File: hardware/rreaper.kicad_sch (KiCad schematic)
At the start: 0 parts

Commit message: added basic hardware schematic
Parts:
- added C11, C22, C31, C41: 100n, symbol Device:C_Small
- added C12: 1u, symbol Device:C_Small
- added C21: 220n, symbol Device:C_Small
- added CJ1: 100n, Capacitor_SMD:C_0805_2012Metric_Pad1.18x1.45mm_HandSolder, symbol Device:C
- added CX1, CX2: 22p, symbol Device:C_Small
- added J1: ZIF, symbol Connector_Generic:Conn_02x14_Counter_Clockwise
- added J2: USB_B_Micro, Connector_USB:USB_Micro-B_Wuerth_629105150521_CircularHoles, symbol Connector:USB_B_Micro
- added J3: ICP, Connector_IDC:IDC-Header_2x05_P2.54mm_Vertical, symbol Connector_Generic:Conn_02x05_Odd_Even
- added R1, R11, R2: 4k7, symbol Device:R_Small
- added U1: ATmega328P, PCM_Package_DIP_AKL:DIP-28_W7.62mm_Socket, symbol MCU_Microchip_ATmega:ATmega328P-P
- added U2: MCP2221A, PCM_Package_DIP_AKL:DIP-14_W7.62mm_Socket, symbol Interface_USB:MCP2221AxP
- added U3, U4: 74HC595, PCM_Package_DIP_AKL:DIP-16_W7.62mm_Socket, symbol 74xx:74HC595
- added X1: 16MHz, symbol PCM_Crystal_AKL:Crystal_Generic
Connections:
- new net: CX1.1, U1.9 (XTAL1/PB6), X1.1
- new net: CX2.1, U1.10 (XTAL2/PB7), X1.2
- new net: R1.1, U3.10 (~{SRCLR})
- new net: U3.9 (QH'), U4.14 (SER)
- new net: C21.1, U2.11 (VUSB)
- new net: J2.2 (D-), U2.12 (D-)
- new net: J2.3 (D+), U2.13 (D+)
- new net: R2.1, U4.10 (~{SRCLR})
- new net +5V: C11.1, C12.1, C22.1, C31.1, C41.1, CJ1.2, J1.28 (Pin_28), J2.1 (VBUS), J3.2 (Pin_2), R1.2, R11.1, R2.2, U1.7 (VCC), U2.1 (VDD), U2.4 (~{RST}), U3.16 (VCC), U4.16 (VCC)
- new net A0: J1.10 (Pin_10), U3.15 (QA)
- new net A1: J1.9 (Pin_9), U3.1 (QB)
- new net A10: J1.21 (Pin_21), U4.2 (QC)
- new net A11: J1.23 (Pin_23), U4.3 (QD)
- new net A12: J1.2 (Pin_2), U4.4 (QE)
- new net A13: J1.26 (Pin_26), U4.5 (QF)
- new net A14: J1.1 (Pin_1), U4.6 (QG)
- new net A15: U4.7 (QH)
- new net A2: J1.8 (Pin_8), U3.2 (QC)
- new net A3: J1.7 (Pin_7), U3.3 (QD)
- new net A4: J1.6 (Pin_6), U3.4 (QE)
- new net A5: J1.5 (Pin_5), U3.5 (QF)
- new net A6: J1.4 (Pin_4), U3.6 (QG)
- new net A7: J1.3 (Pin_3), U3.7 (QH)
- new net A8: J1.25 (Pin_25), U4.15 (QA)
- new net A9: J1.24 (Pin_24), U4.1 (QB)
- new net CE: J1.20 (Pin_20), U1.15 (PB1)
- new net D0: J1.11 (Pin_11), U1.23 (PC0)
- new net D1: J1.12 (Pin_12), U1.24 (PC1)
- new net D2: J1.13 (Pin_13), U1.25 (PC2)
- new net D3: J1.15 (Pin_15), U1.26 (PC3)
- new net D4: J1.16 (Pin_16), U1.27 (PC4)
- new net D5: J1.17 (Pin_17), U1.28 (PC5)
- new net D6: J1.18 (Pin_18), U1.11 (PD5)
- new net D7: J1.19 (Pin_19), U1.12 (PD6)
- new net GND: C11.2, C12.2, C21.2, C22.2, C31.2, C41.2, CJ1.1, CX1.2, CX2.2, J1.14 (Pin_14), J2.5 (GND), J3.10 (Pin_10), J3.3 (Pin_3), J3.4 (Pin_4), J3.6 (Pin_6), J3.8 (Pin_8), U1.22 (GND), U1.8 (GND), U2.14 (VSS), U3.13 (~{OE}), U3.8 (GND), U4.13 (~{OE}), U4.8 (GND)
- new net LATCH: U1.16 (PB2), U3.12 (RCLK), U4.12 (RCLK)
- new net MISO: J3.9 (Pin_9), U1.18 (PB4)
- new net MOSI: J3.1 (Pin_1), U1.17 (PB3), U3.14 (SER)
- new net OE: J1.22 (Pin_22), U1.14 (PB0)
- new net SCK: J3.7 (Pin_7), U1.19 (PB5), U3.11 (SRCLK), U4.11 (SRCLK)
- new net UART_{MCU->PC}: U1.3 (PD1), U2.5 (URx)
- new net UART_{PC->MCU}: U1.2 (PD0), U2.6 (UTx)
- new net WE: J1.27 (Pin_27), U1.13 (PD7)
- new net ~{RST}: J3.5 (Pin_5), R11.2, U1.1 (~{RESET}/PC6)
- no-connect marks 0 -> 10
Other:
- note added: "Address Bus Accumulator"
- note added: "EEPROM Socket"
- note added: "MCU"
- note added: "Power & External Communication"

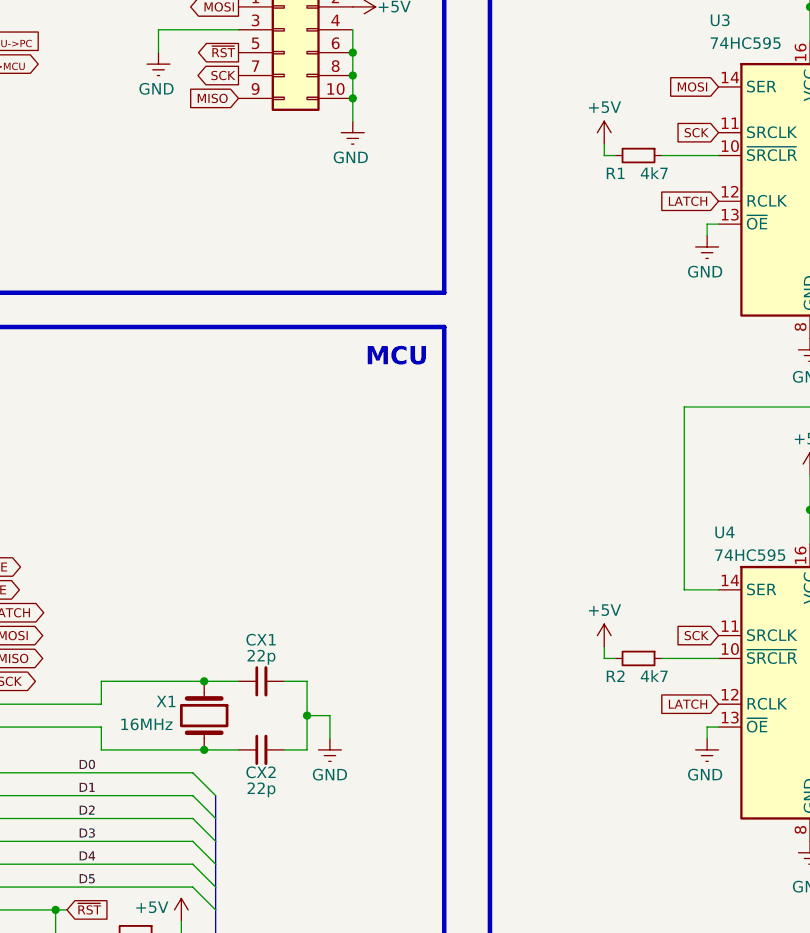
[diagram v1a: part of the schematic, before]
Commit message: added basic PCB layout
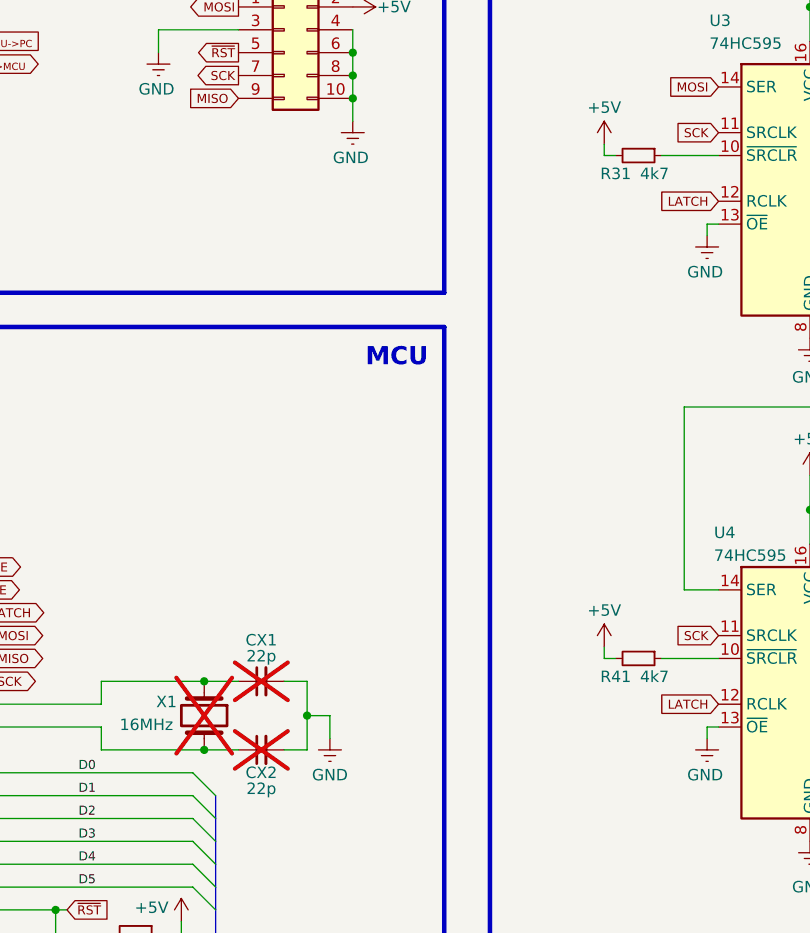
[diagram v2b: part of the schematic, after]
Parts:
- C11, C12, C21, C22, C31, C41: footprint (none) -> Capacitor_THT:C_Disc_D5.0mm_W2.5mm_P2.50mm
- CJ1: footprint Capacitor_SMD:C_0805_2012Metric_Pad1.18x1.45mm_HandSolder -> Capacitor_THT:C_Disc_D5.0mm_W2.5mm_P2.50mm
- CX1, CX2: footprint (none) -> Capacitor_THT:C_Disc_D5.0mm_W2.5mm_P2.50mm; now not fitted; now left out of the parts list
- J1: footprint (none) -> Socket:DIP_Socket-28_W11.9_W12.7_W15.24_W17.78_W18.5_3M_228-1277-00-0602J
- R11: footprint (none) -> PCM_Resistor_THT_AKL:R_Axial_DIN0207_L6.3mm_D2.5mm_P10.16mm_Horizontal
- R31: renamed from R1; footprint (none) -> PCM_Resistor_THT_AKL:R_Axial_DIN0207_L6.3mm_D2.5mm_P10.16mm_Horizontal
- R41: renamed from R2; footprint (none) -> PCM_Resistor_THT_AKL:R_Axial_DIN0207_L6.3mm_D2.5mm_P10.16mm_Horizontal
- X1: footprint (none) -> Crystal:Crystal_HC18-U_Vertical; now not fitted; now left out of the parts list
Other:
- company: (none) -> virtualgrub39
- title: (none) -> Atmega328P 28C64/28C256 USB EEPROM programmer
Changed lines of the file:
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@@
 	(generator_version "9.0")
 	(paper "A4")
+	(title_block
+		(title "Atmega328P 28C64/28C256 USB EEPROM programmer")
+		(rev "1")
+		(company "virtualgrub39")
+	)
 	(rectangle
 		(start 196.85 13.97)
@@
 		(unit 1)
 		(exclude_from_sim no)
-		(in_bom yes)
+		(in_bom no)
 		(on_board yes)
-		(dnp no)
+		(dnp yes)
 		(property "Reference" "CX1"
 			(at 99.06 109.728 90)
@@
 			)
 		)
-		(property "Footprint" ""
+		(property "Footprint" "Capacitor_THT:C_Disc_D5.0mm_W2.5mm_P2.50mm"
 			(at 99.06 114.3 0)
 			(effects
@@
 			)
 		)
-		(property "Footprint" ""
+		(property "Footprint" "Capacitor_THT:C_Disc_D5.0mm_W2.5mm_P2.50mm"
 			(at 58.42 87.63 0)
 			(effects
@@
 			)
 		)
-		(property "Footprint" ""
+		(property "Footprint" "Capacitor_THT:C_Disc_D5.0mm_W2.5mm_P2.50mm"
 			(at 165.1 39.37 0)
 			(effects
@@
 		(unit 1)
 		(exclude_from_sim no)
-		(in_bom yes)
+		(in_bom no)
 		(on_board yes)
-		(dnp no)
+		(dnp yes)
 		(property "Reference" "X1"
 			(at 87.376 116.586 90)
@@
 			)
 		)
-		(property "Footprint" ""
+		(property "Footprint" "Crystal:Crystal_HC18-U_Vertical"
 			(at 92.71 118.11 0)
 			(effects
@@
 			)
 		)
-		(property "Footprint" ""
+		(property "Footprint" "Socket:DIP_Socket-28_W11.9_W12.7_W15.24_W17.78_W18.5_3M_228-1277-00-0602J"
 			(at 229.87 81.28 0)
 			(effects
@@
 			)
 		)
-		(property "Footprint" ""
+		(property "Footprint" "Capacitor_THT:C_Disc_D5.0mm_W2.5mm_P2.50mm"
 			(at 60.96 27.94 0)
 			(effects
@@
 			)
 		)
-		(property "Footprint" ""
+		(property "Footprint" "Capacitor_THT:C_Disc_D5.0mm_W2.5mm_P2.50mm"
 			(at 58.42 83.82 0)
 			(effects
@@
 		(on_board yes)
 		(dnp no)
-		(property "Reference" "R2"
+		(property "Reference" "R41"
 			(at 138.43 113.792 90)
 			(effects
@@
 			)
 		)
-		(property "Footprint" ""
+		(property "Footprint" "PCM_Resistor_THT_AKL:R_Axial_DIN0207_L6.3mm_D2.5mm_P10.16mm_Horizontal"
 			(at 140.97 111.76 0)
 			(effects
@@
 			(project "rreaper"
 				(path "/061140d5-a8b8-4992-87a0-22d4d4897d8f"
-					(reference "R2")
+					(reference "R41")
 					(unit 1)
 				)
@@
 			)
 		)
-		(property "Footprint" "Capacitor_SMD:C_0805_2012Metric_Pad1.18x1.45mm_HandSolder"
+		(property "Footprint" "Capacitor_THT:C_Disc_D5.0mm_W2.5mm_P2.50mm"
 			(at 250.4948 69.85 0)
 			(effects
@@
 			)
 		)
-		(property "Footprint" ""
+		(property "Footprint" "PCM_Resistor_THT_AKL:R_Axial_DIN0207_L6.3mm_D2.5mm_P10.16mm_Horizontal"
 			(at 85.09 142.24 0)
 			(effects
@@
 		(unit 1)
 		(exclude_from_sim no)
-		(in_bom yes)
+		(in_bom no)
 		(on_board yes)
-		(dnp no)
+		(dnp yes)
 		(property "Reference" "CX2"
 			(at 99.06 124.46 90)
@@
 			)
 		)
-		(property "Footprint" ""
+		(property "Footprint" "Capacitor_THT:C_Disc_D5.0mm_W2.5mm_P2.50mm"
 			(at 99.06 121.92 0)
 			(effects
@@
 		(on_board yes)
 		(dnp no)
-		(property "Reference" "R1"
+		(property "Reference" "R31"
 			(at 138.43 57.912 90)
 			(effects
@@
 			)
 		)
-		(property "Footprint" ""
+		(property "Footprint" "PCM_Resistor_THT_AKL:R_Axial_DIN0207_L6.3mm_D2.5mm_P10.16mm_Horizontal"
 			(at 140.97 55.88 0)
 			(effects
@@
 			(project "rreaper"
 				(path "/061140d5-a8b8-4992-87a0-22d4d4897d8f"
-					(reference "R1")
+					(reference "R31")
 					(unit 1)
 				)
@@
 			)
 		)
-		(property "Footprint" ""
+		(property "Footprint" "Capacitor_THT:C_Disc_D5.0mm_W2.5mm_P2.50mm"
 			(at 60.96 24.13 0)
 			(effects
@@
 			)
 		)
-		(property "Footprint" ""
+		(property "Footprint" "Capacitor_THT:C_Disc_D5.0mm_W2.5mm_P2.50mm"
 			(at 165.1 95.25 0)
 			(effects

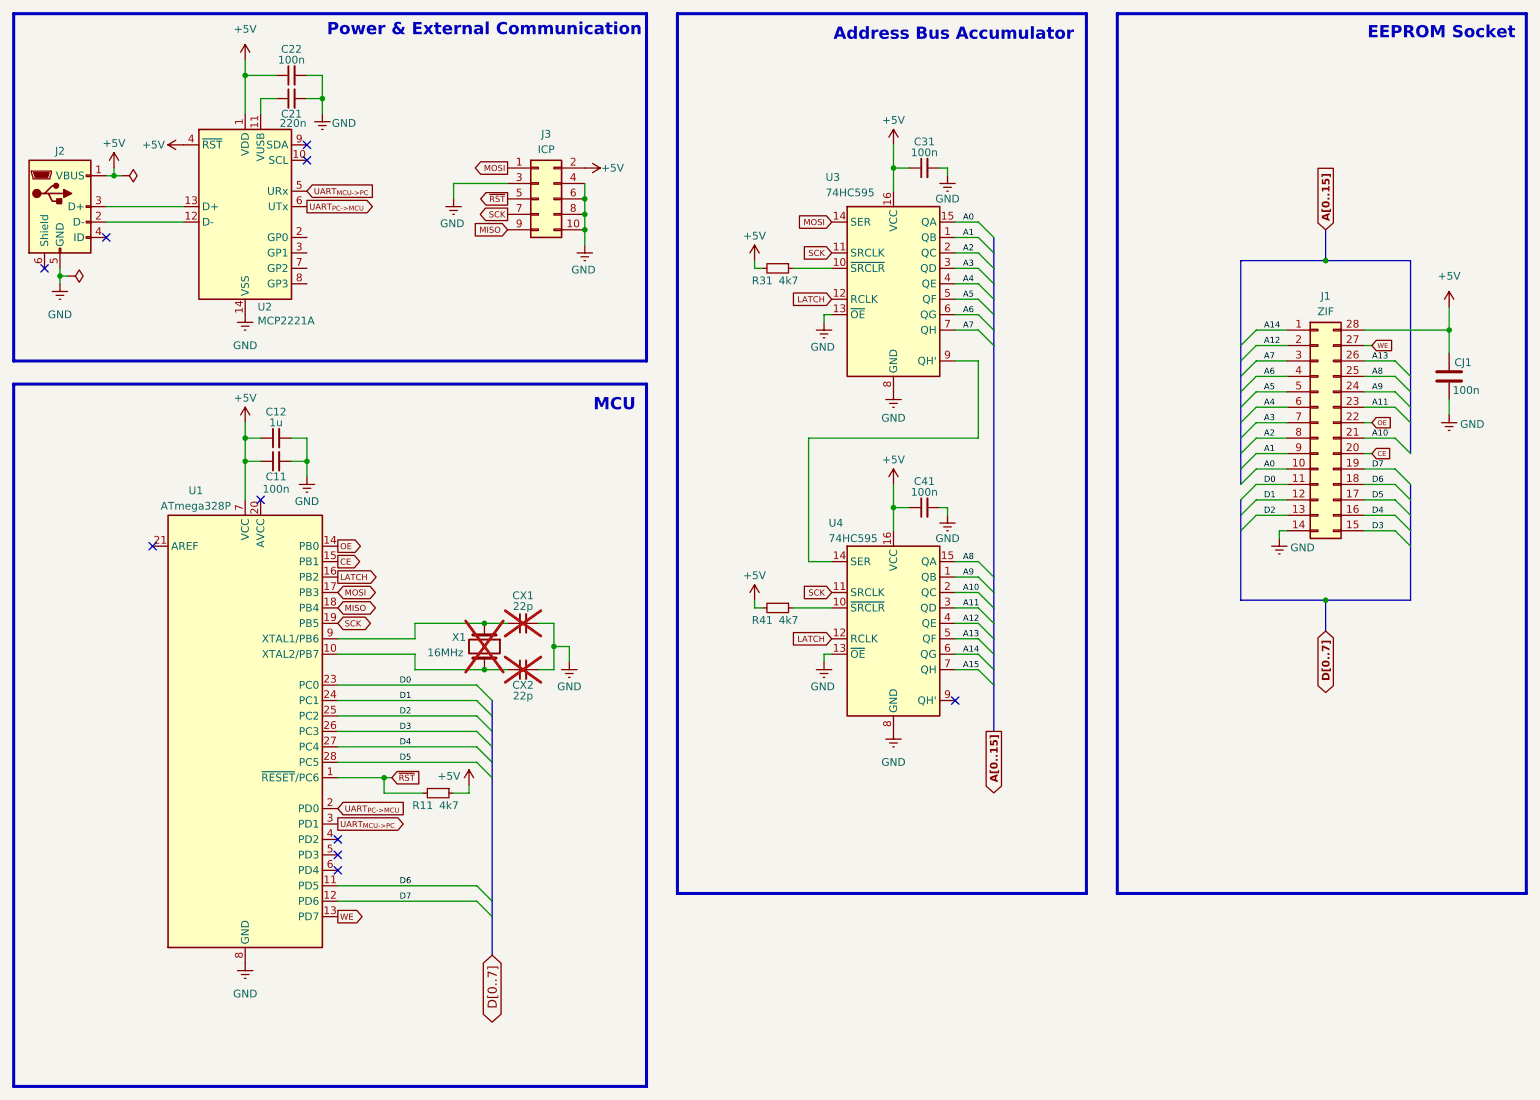
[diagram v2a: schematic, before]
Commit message: completed first PCB layout
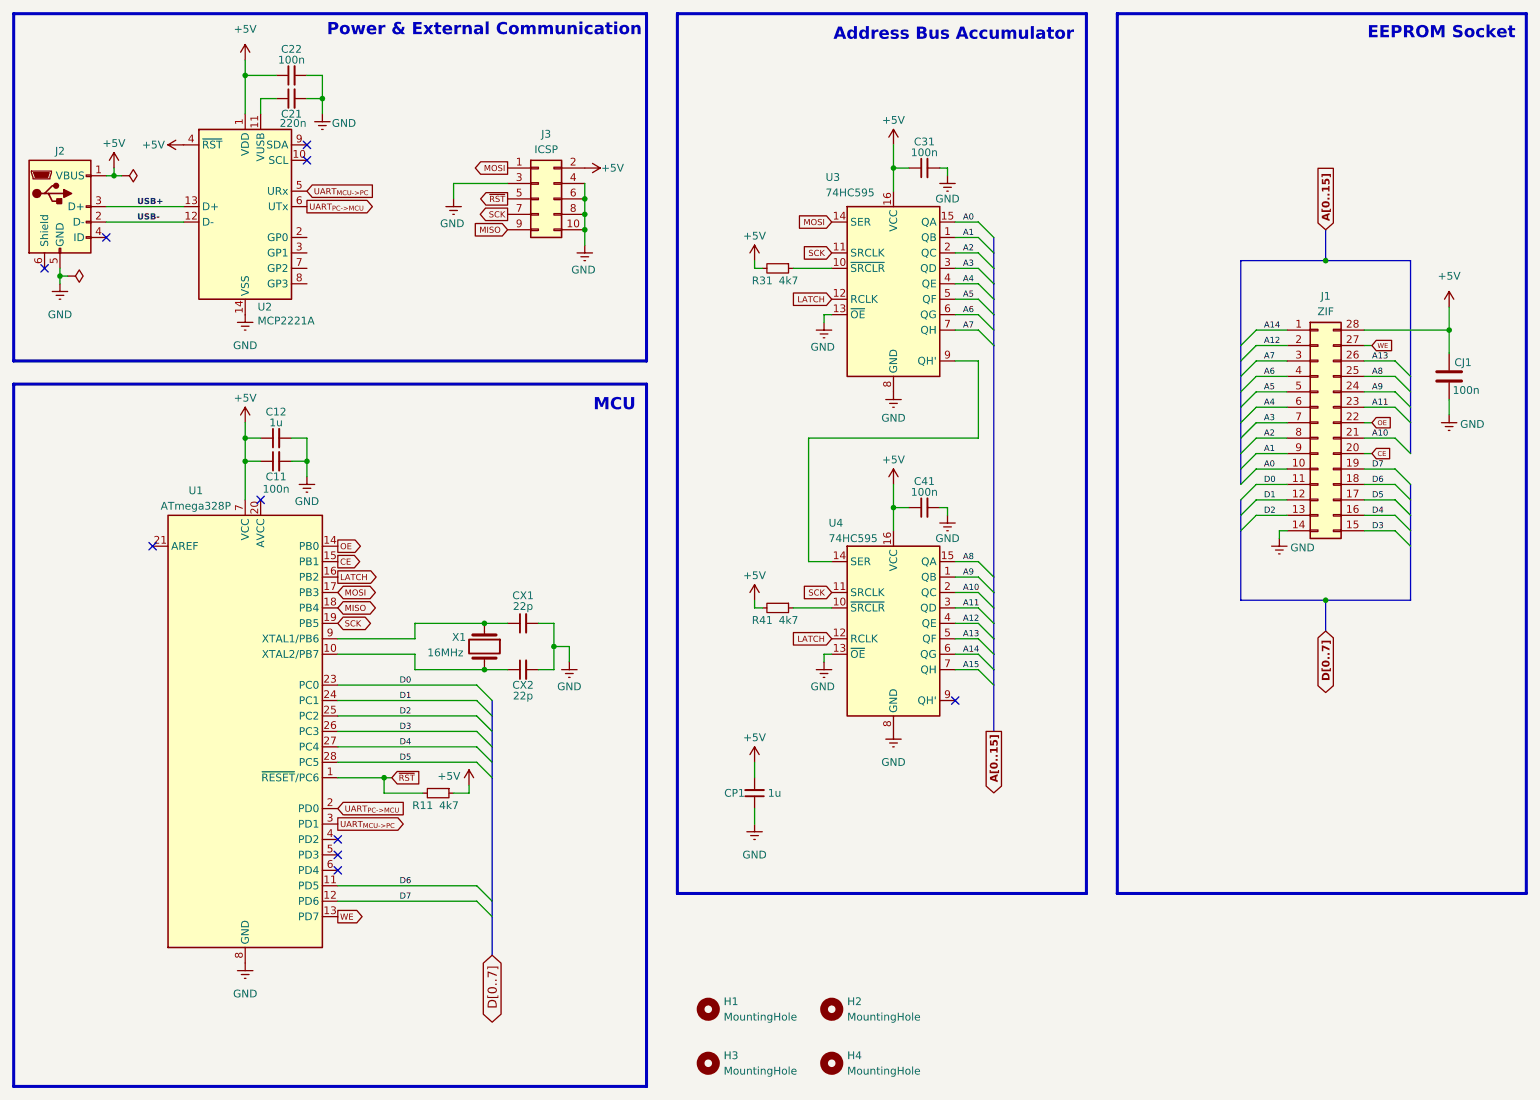
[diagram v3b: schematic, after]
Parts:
- added CP1: 1u, Capacitor_THT:C_Disc_D5.0mm_W2.5mm_P2.50mm, symbol Device:C_Small
- added H1, H2, H3, H4: MountingHole, MountingHole:MountingHole_2.7mm_M2.5, symbol Mechanical:MountingHole
- CX1, CX2, X1: now fitted; now in the parts list
- J3: value ICP -> ICSP
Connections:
- net +5V: now also CP1.2
- net GND: now also CP1.1
- net USB-: now reaches J2.2 (D-), U2.12 (D-)
- net USB+: now reaches J2.3 (D+), U2.13 (D+)
